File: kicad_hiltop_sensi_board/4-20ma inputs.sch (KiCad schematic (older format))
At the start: 44 parts, among them U16 MAX4194

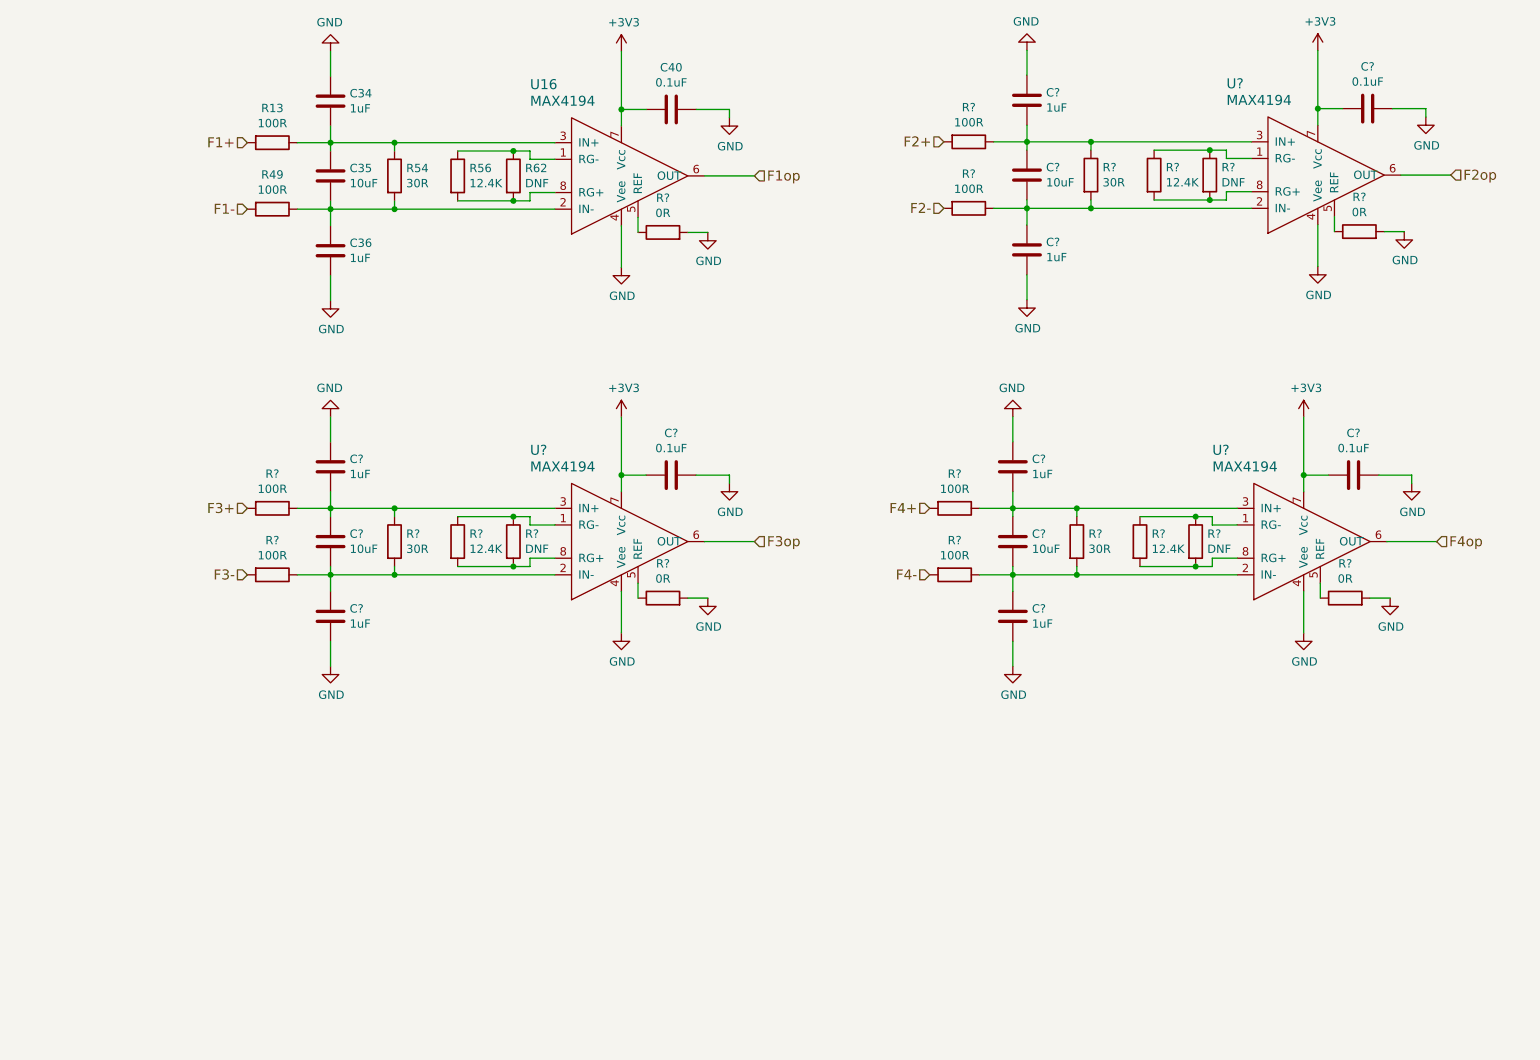
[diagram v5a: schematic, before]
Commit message: Sensi board schematic updated from comments
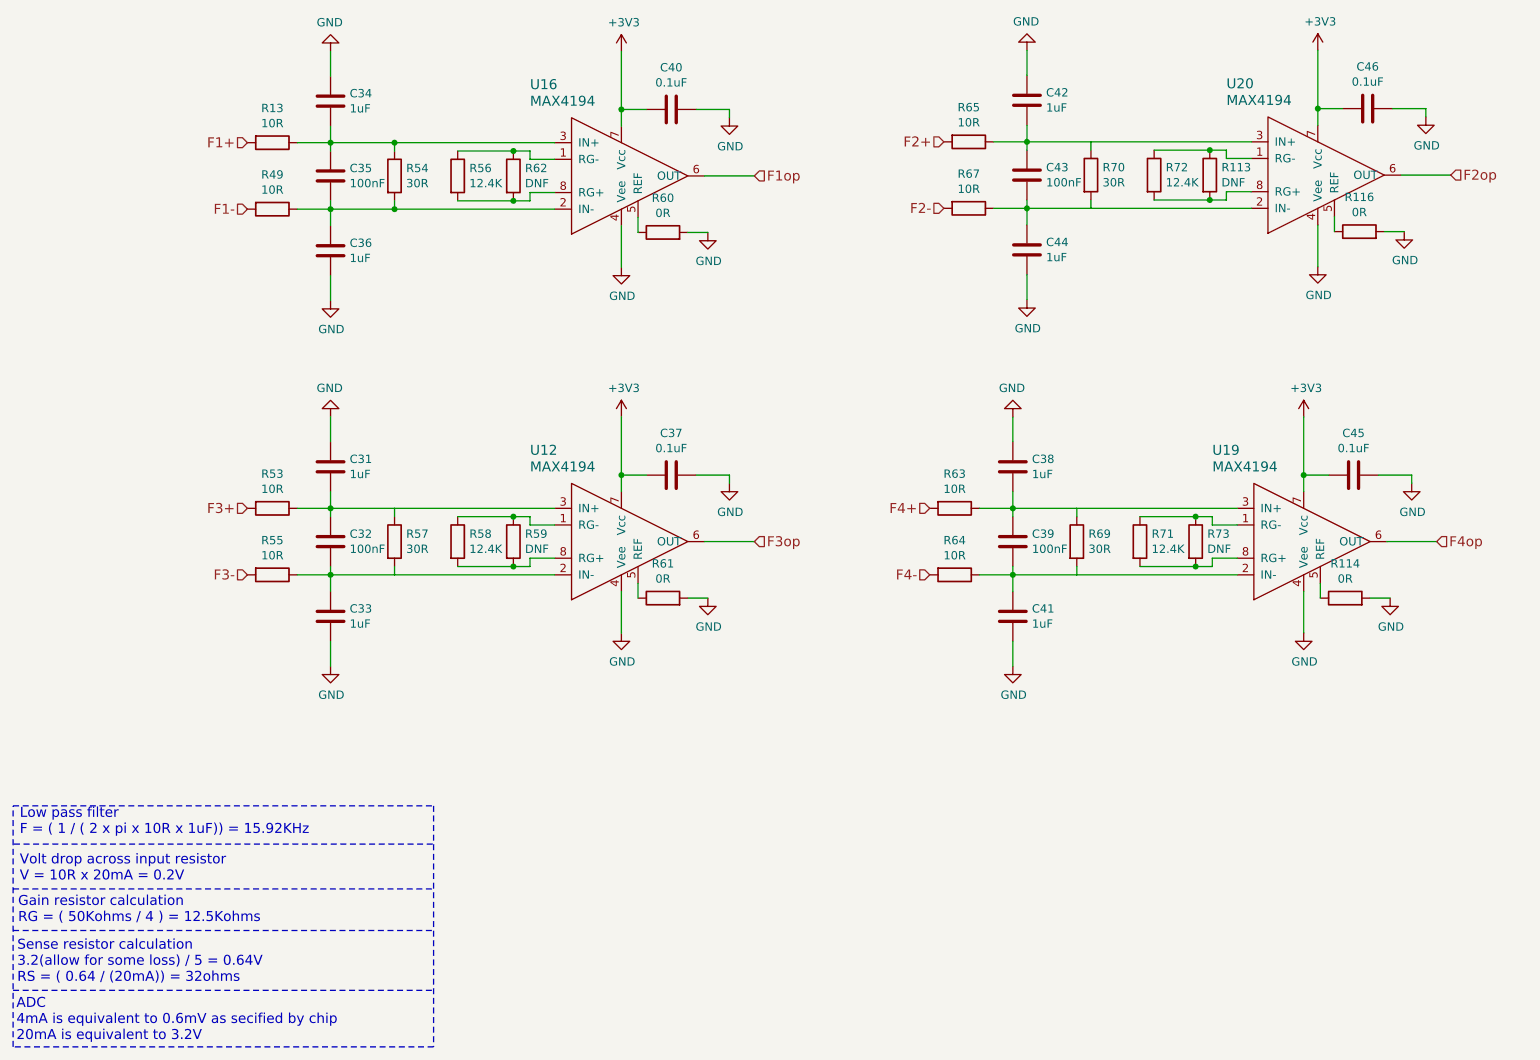
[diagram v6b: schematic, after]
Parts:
- removed C? (x3): 10uF, Capacitor_SMD:C_0603_1608Metric, symbol device:C
- removed C? (x6): 1uF, Capacitor_SMD:C_0603_1608Metric, symbol device:C
- removed R? (x6): 100R, Resistor_SMD:R_0603_1608Metric, symbol device:R
- added C31, C33, C38, C41, C42, C44: 1uF, Capacitor_SMD:C_0603_1608Metric, symbol device:C
- added C32, C39, C43: 100nF, Capacitor_SMD:C_0603_1608Metric, symbol device:C
- added R53, R55, R63, R64, R65, R67: 10R, Resistor_SMD:R_0603_1608Metric, symbol device:R
- C35: value 10uF -> 100nF
- R13, R49: value 100R -> 10R
- R54: Devtank 101-054 -> 103-004; Tolerance (none) -> 0.1%
- R57, R69, R70: renamed from R?; Devtank 101-054 -> 103-004; Tolerance (none) -> 0.1%
- gave numbers to parts that had none: 16
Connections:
- net F2+: now also R65.2
- net F2-: now also R67.2
- net F3+: now also R53.2
- net F3-: now also R55.2
- net F4+: now also R63.2
- net F4-: now also R64.2
- net GND: now also C31.1, C33.2, C38.1, C41.2, C42.1, C44.2
- net at R70.2, U20.2 (IN-): now also C43.2, C44.1, R67.1
- net at R70.1, U20.3 (IN+): now also C42.2, C43.1, R65.1
- net at R57.2, U12.2 (IN-): now also C32.2, C33.1, R55.1
- net at R57.1, U12.3 (IN+): now also C31.2, C32.1, R53.1
- net at R69.2, U19.2 (IN-): now also C39.2, C41.1, R64.1
- net at R69.1, U19.3 (IN+): now also C38.2, C39.1, R63.1
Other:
- note added: "ADC\n4mA is equivalent to 0.6mV as secified by chip\n20mA is equivalent to 3.2V"
- note added: "Gain resistor calculation\nRG = ( 50Kohms / 4 ) = 12.5Kohms"
- note added: "Low pass filter\nF = ( 1 / ( 2 x pi x 10R x 1uF)) = 15.92KHz\n"
- note added: "Sense resistor calculation\n3.2(allow for some loss) / 5 = 0.64V\nRS = ( 0.64 / (20mA)) = 32ohms\n"
- note added: "Volt drop across input resistor\nV = 10R x 20mA = 0.2V"

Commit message: Updated sensi board layout
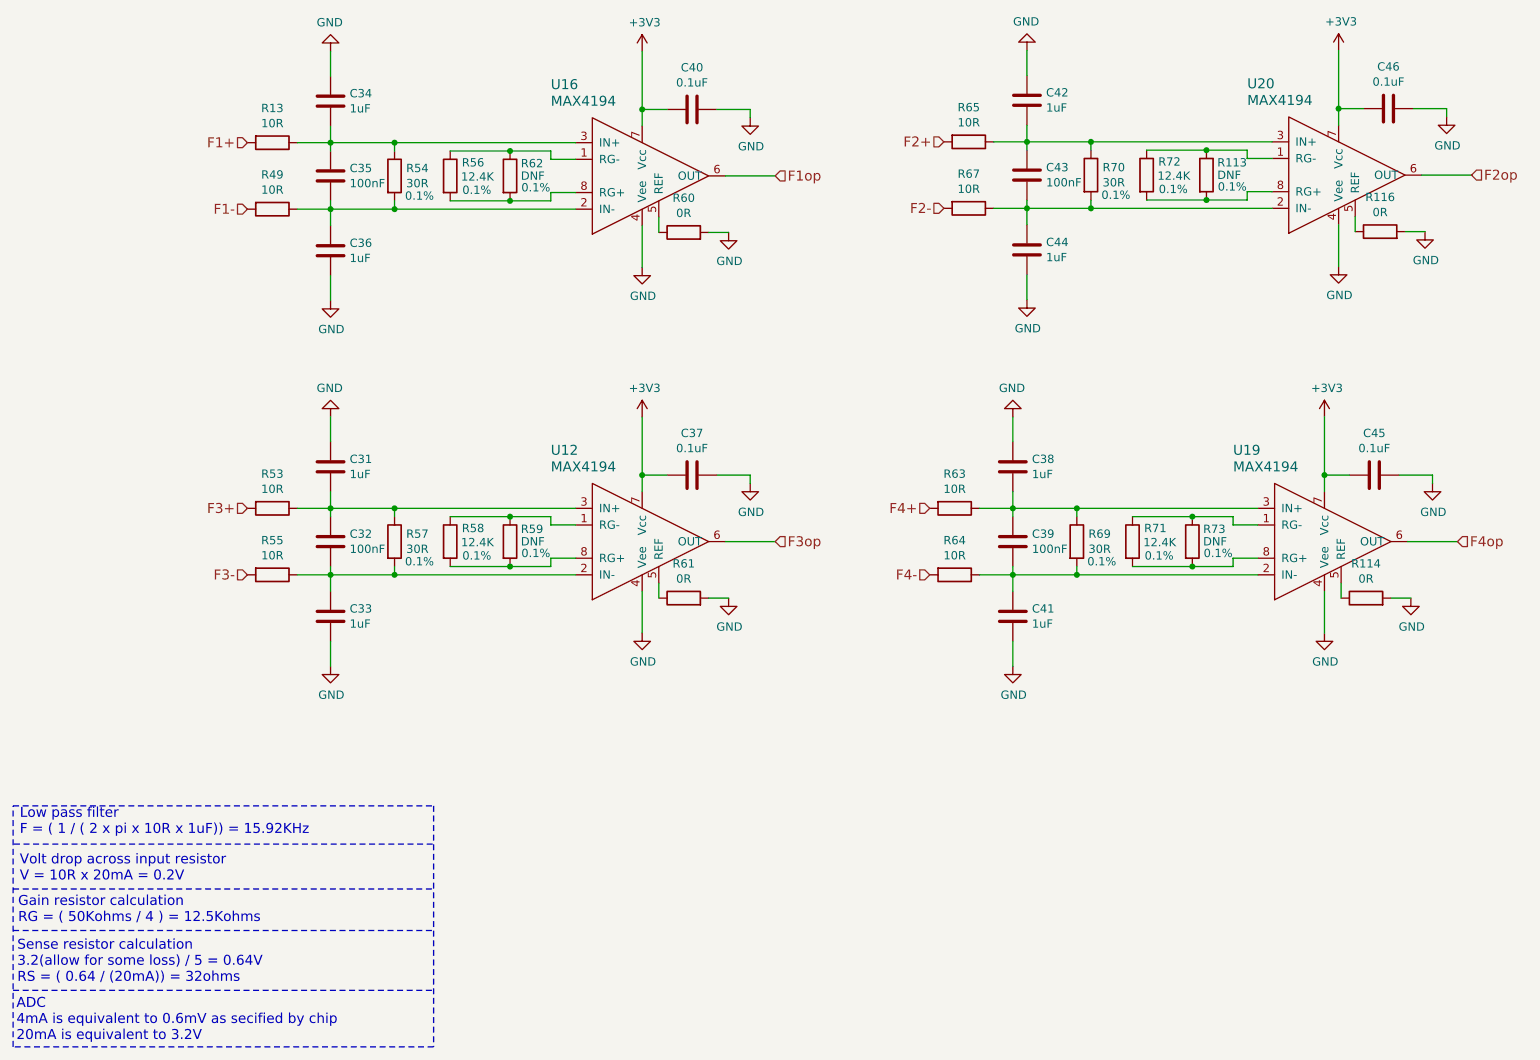
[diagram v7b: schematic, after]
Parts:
- R114, R116, R60, R61: footprint (none) -> Resistor_SMD:R_0603_1608Metric
- R56, R58, R71, R72: Tolerance (none) -> 0.1%
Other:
- moved on the sheet: C40, R56, R60, R62, U16

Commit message: Sensi Board Complete
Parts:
- C31, C33, C34, C36, C38, C41, C42, C44: Devtank (none) -> 105-027
- C32, C35, C39, C43: Devtank (none) -> 105-002
- R114, R116, R60, R61: Devtank (none) -> 101-005
- R13, R49, R53, R55, R63, R64, R65, R67: Devtank (none) -> 101-058
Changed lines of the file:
@@
 F 2 "Capacitor_SMD:C_0603_1608Metric" H 2788 2100 50  0001 C CNN
 F 3 "" H 2750 2250 50  0001 C CNN
+F 4 "105-002" H 2750 2250 50  0001 C CNN "Devtank"
 	1    2750 2250
 	1    0    0    -1
@@
 F 2 "Capacitor_SMD:C_0603_1608Metric" H 2788 1650 50  0001 C CNN
 F 3 "" H 2750 1800 50  0001 C CNN
+F 4 "105-027" H 2750 1800 50  0001 C CNN "Devtank"
 	1    2750 1800
 	1    0    0    -1
@@
 F 2 "Capacitor_SMD:C_0603_1608Metric" H 2788 2550 50  0001 C CNN
 F 3 "" H 2750 2700 50  0001 C CNN
+F 4 "105-027" H 2750 2700 50  0001 C CNN "Devtank"
 	1    2750 2700
 	1    0    0    -1
@@
 F 2 "Resistor_SMD:R_0603_1608Metric" V 2330 2050 50  0001 C CNN
 F 3 "" H 2400 2050 50  0001 C CNN
+F 4 "101-058" H 2400 2050 50  0001 C CNN "Devtank"
 	1    2400 2050
 	0    1    1    0
@@
 F 2 "Resistor_SMD:R_0603_1608Metric" V 2330 2450 50  0001 C CNN
 F 3 "" H 2400 2450 50  0001 C CNN
+F 4 "101-058" H 2400 2450 50  0001 C CNN "Devtank"
 	1    2400 2450
 	0    1    1    0
@@
 F 2 "Resistor_SMD:R_0603_1608Metric" V 4805 2590 50  0001 C CNN
 F 3 "" H 4875 2590 50  0001 C CNN
+F 4 "101-005" H 4875 2590 50  0001 C CNN "Devtank"
 	1    4875 2590
 	0    -1   -1   0
@@
 F 2 "Capacitor_SMD:C_0603_1608Metric" H 6978 2095 50  0001 C CNN
 F 3 "" H 6940 2245 50  0001 C CNN
+F 4 "105-002" H 6940 2245 50  0001 C CNN "Devtank"
 	1    6940 2245
 	1    0    0    -1
@@
 F 2 "Capacitor_SMD:C_0603_1608Metric" H 6978 1645 50  0001 C CNN
 F 3 "" H 6940 1795 50  0001 C CNN
+F 4 "105-027" H 6940 1795 50  0001 C CNN "Devtank"
 	1    6940 1795
 	1    0    0    -1
@@
 F 2 "Capacitor_SMD:C_0603_1608Metric" H 6978 2545 50  0001 C CNN
 F 3 "" H 6940 2695 50  0001 C CNN
+F 4 "105-027" H 6940 2695 50  0001 C CNN "Devtank"
 	1    6940 2695
 	1    0    0    -1
@@
 F 2 "Resistor_SMD:R_0603_1608Metric" V 6520 2045 50  0001 C CNN
 F 3 "" H 6590 2045 50  0001 C CNN
+F 4 "101-058" H 6590 2045 50  0001 C CNN "Devtank"
 	1    6590 2045
 	0    1    1    0
@@
 F 2 "Resistor_SMD:R_0603_1608Metric" V 6520 2445 50  0001 C CNN
 F 3 "" H 6590 2445 50  0001 C CNN
+F 4 "101-058" H 6590 2445 50  0001 C CNN "Devtank"
 	1    6590 2445
 	0    1    1    0
@@
 F 2 "Resistor_SMD:R_0603_1608Metric" V 8995 2585 50  0001 C CNN
 F 3 "" H 9065 2585 50  0001 C CNN
+F 4 "101-005" H 9065 2585 50  0001 C CNN "Devtank"
 	1    9065 2585
 	0    -1   -1   0
@@
 F 2 "Capacitor_SMD:C_0603_1608Metric" H 2788 4300 50  0001 C CNN
 F 3 "" H 2750 4450 50  0001 C CNN
+F 4 "105-002" H 2750 4450 50  0001 C CNN "Devtank"
 	1    2750 4450
 	1    0    0    -1
@@
 F 2 "Capacitor_SMD:C_0603_1608Metric" H 2788 3850 50  0001 C CNN
 F 3 "" H 2750 4000 50  0001 C CNN
+F 4 "105-027" H 2750 4000 50  0001 C CNN "Devtank"
 	1    2750 4000
 	1    0    0    -1
@@
 F 2 "Capacitor_SMD:C_0603_1608Metric" H 2788 4750 50  0001 C CNN
 F 3 "" H 2750 4900 50  0001 C CNN
+F 4 "105-027" H 2750 4900 50  0001 C CNN "Devtank"
 	1    2750 4900
 	1    0    0    -1
@@
 F 2 "Resistor_SMD:R_0603_1608Metric" V 2330 4250 50  0001 C CNN
 F 3 "" H 2400 4250 50  0001 C CNN
+F 4 "101-058" H 2400 4250 50  0001 C CNN "Devtank"
 	1    2400 4250
 	0    1    1    0
@@
 F 2 "Resistor_SMD:R_0603_1608Metric" V 2330 4650 50  0001 C CNN
 F 3 "" H 2400 4650 50  0001 C CNN
+F 4 "101-058" H 2400 4650 50  0001 C CNN "Devtank"
 	1    2400 4650
 	0    1    1    0
@@
 F 2 "Resistor_SMD:R_0603_1608Metric" V 4805 4790 50  0001 C CNN
 F 3 "" H 4875 4790 50  0001 C CNN
+F 4 "101-005" H 4875 4790 50  0001 C CNN "Devtank"
 	1    4875 4790
 	0    -1   -1   0
@@
 F 2 "Capacitor_SMD:C_0603_1608Metric" H 6893 4300 50  0001 C CNN
 F 3 "" H 6855 4450 50  0001 C CNN
+F 4 "105-002" H 6855 4450 50  0001 C CNN "Devtank"
 	1    6855 4450
 	1    0    0    -1
@@
 F 2 "Capacitor_SMD:C_0603_1608Metric" H 6893 3850 50  0001 C CNN
 F 3 "" H 6855 4000 50  0001 C CNN
+F 4 "105-027" H 6855 4000 50  0001 C CNN "Devtank"
 	1    6855 4000
 	1    0    0    -1
@@
 F 2 "Capacitor_SMD:C_0603_1608Metric" H 6893 4750 50  0001 C CNN
 F 3 "" H 6855 4900 50  0001 C CNN
+F 4 "105-027" H 6855 4900 50  0001 C CNN "Devtank"
 	1    6855 4900
 	1    0    0    -1
@@
 F 2 "Resistor_SMD:R_0603_1608Metric" V 6435 4250 50  0001 C CNN
 F 3 "" H 6505 4250 50  0001 C CNN
+F 4 "101-058" H 6505 4250 50  0001 C CNN "Devtank"
 	1    6505 4250
 	0    1    1    0
@@
 F 2 "Resistor_SMD:R_0603_1608Metric" V 6435 4650 50  0001 C CNN
 F 3 "" H 6505 4650 50  0001 C CNN
+F 4 "101-058" H 6505 4650 50  0001 C CNN "Devtank"
 	1    6505 4650
 	0    1    1    0
@@
 F 2 "Resistor_SMD:R_0603_1608Metric" V 8910 4790 50  0001 C CNN
 F 3 "" H 8980 4790 50  0001 C CNN
+F 4 "101-005" H 8980 4790 50  0001 C CNN "Devtank"
 	1    8980 4790
 	0    -1   -1   0
